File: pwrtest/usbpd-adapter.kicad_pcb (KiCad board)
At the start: 2 copper layers, 61.2 x 27 mm, 30 parts, among them J1 Conn_01x04, J2 Conn_01x04, J3 USB_C_Receptacle_USB2.0_16P, Q1 AO3400A, U1 AP63205WU, U2 L7812, U3 IP2721

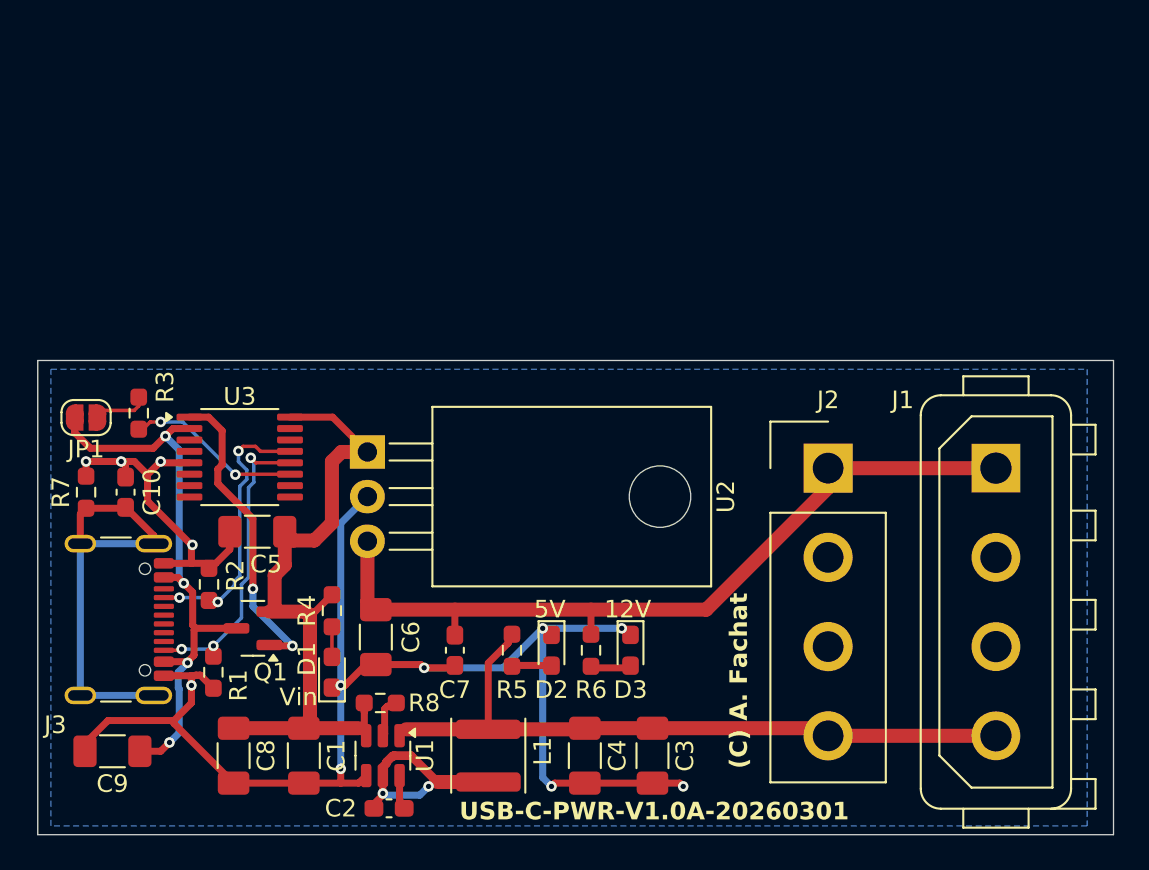
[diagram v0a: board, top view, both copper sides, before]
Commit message: usb power adapter 1.1a
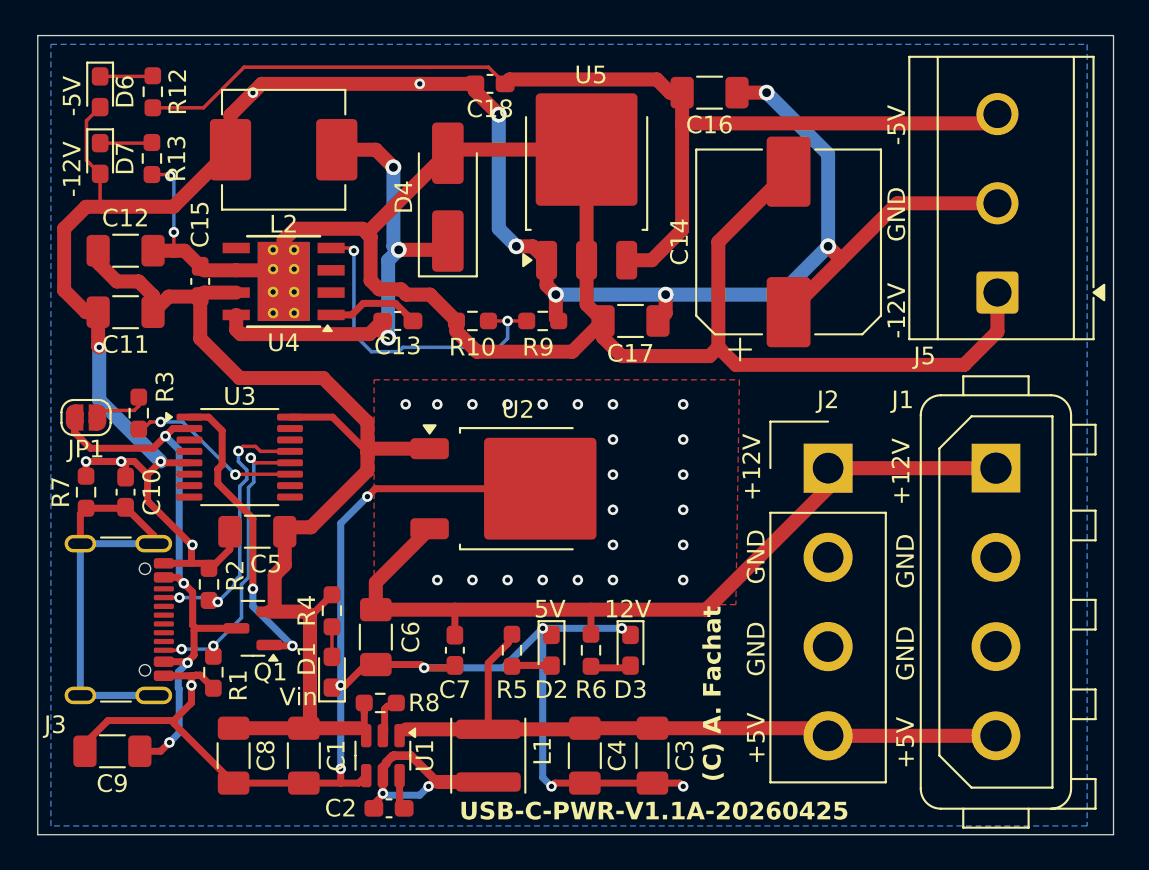
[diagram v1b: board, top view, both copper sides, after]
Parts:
- added C11: 10u, Capacitor_SMD:C_1206_3216Metric_Pad1.33x1.80mm_HandSolder, F.Cu at (90.2, 70.8)
- added C12: 10u, Capacitor_SMD:C_1206_3216Metric_Pad1.33x1.80mm_HandSolder, F.Cu at (90.2, 67.2)
- added C13: 0.01uF low ESR, Capacitor_SMD:C_0603_1608Metric_Pad1.08x0.95mm_HandSolder, F.Cu at (105.8, 71.2)
- added C14: 220u, Capacitor_SMD:CP_Elec_10x10, F.Cu at (128.0, 66.8)
- added C15: 100n, Capacitor_SMD:C_0603_1608Metric_Pad1.08x0.95mm_HandSolder, F.Cu at (94.5, 69.0)
- added C16: 22u, Capacitor_SMD:C_1206_3216Metric_Pad1.33x1.80mm_HandSolder, F.Cu at (123.5, 58.2)
- added C17: 10u, Capacitor_SMD:C_1206_3216Metric_Pad1.33x1.80mm_HandSolder, F.Cu at (119.0, 71.2)
- added C18: 100n, Capacitor_SMD:C_0603_1608Metric_Pad1.08x0.95mm_HandSolder, F.Cu at (111.0, 57.8)
- added D4: B340A, Diode_SMD:D_SMA_Handsoldering, F.Cu at (108.6, 64.2)
- added D6: LED, Diode_SMD:D_0603_1608Metric_Pad1.05x0.95mm_HandSolder, F.Cu at (88.8, 58.2)
- added D7: LED, Diode_SMD:D_0603_1608Metric_Pad1.05x0.95mm_HandSolder, F.Cu at (88.8, 62.0)
- added J5: Screw_Terminal_01x03, TerminalBlock_CUI:TerminalBlock_CUI_TB007-508-03_1x03_P5.08mm_Horizontal, F.Cu at (139.9, 69.6)
- added L2: 15uH, Inductor_SMD:L_APV_APH0630, F.Cu at (99.2, 61.5)
- added R10: 1.13k, Resistor_SMD:R_0603_1608Metric_Pad0.98x0.95mm_HandSolder, F.Cu at (110.0, 71.2)
- added R12: 620, Resistor_SMD:R_0603_1608Metric_Pad0.98x0.95mm_HandSolder, F.Cu at (91.8, 58.2)
- added R13: 2k, Resistor_SMD:R_0603_1608Metric_Pad0.98x0.95mm_HandSolder, F.Cu at (91.8, 62.0)
- added R9: 100k, Resistor_SMD:R_0603_1608Metric_Pad0.98x0.95mm_HandSolder, F.Cu at (114.0, 71.2)
- added U4: TPS5430DDA, Package_SO:TI_SO-PowerPAD-8_ThermalVias, F.Cu at (99.2, 69.0)
- added U5: L7905, Package_TO_SOT_SMD:TO-252-3_TabPin2, F.Cu at (116.5, 62.8)
- U2: footprint Package_TO_SOT_THT:TO-220-3_Horizontal_TabDown -> Package_TO_SOT_SMD:TO-252-2
- moved U2 8.83 mm to (112.6, 80.8), turned to 0 degrees
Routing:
- net GND: track 99.3 -> 221.5 mm, vias 12 -> 45
- net -12V: track 0.00 -> 103.6 mm, vias 0 -> 2
- net -5V: track 0.00 -> 61.8 mm
- net Net-(D4-K): track 0.00 -> 28.5 mm, vias 0 -> 3
- net VIN: track 39.7 -> 67.8 mm
- net Net-(U4-VSENSE): track 0.00 -> 18.8 mm, vias 0 -> 2
- net Net-(U4-BOOT): track 0.00 -> 5.35 mm
- net Net-(D6-K): track 0.00 -> 3.02 mm
- net Net-(D7-K): track 0.00 -> 2.97 mm
- net 12V: track 46.2 -> 48.0 mm
- added copper zone on F.Cu, net GND
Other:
- board size 61.2 x 27 mm -> 61.2 x 45.5 mm
- board text added: "+12V"
- board text added: "+5V"
- board text added: "-12V"
- board text added: "-5V"
- board text added: "GND"
- board text added: "USB-C-PWR-V1.1A-20260425"
- board text removed: "USB-C-PWR-V1.0A-20260301"

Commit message: update wrong resistors in pwrtest board
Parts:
- R10: value 1.13k -> 1.1k
- R9: value 100k -> 10k
